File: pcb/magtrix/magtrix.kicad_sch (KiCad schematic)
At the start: 0 parts

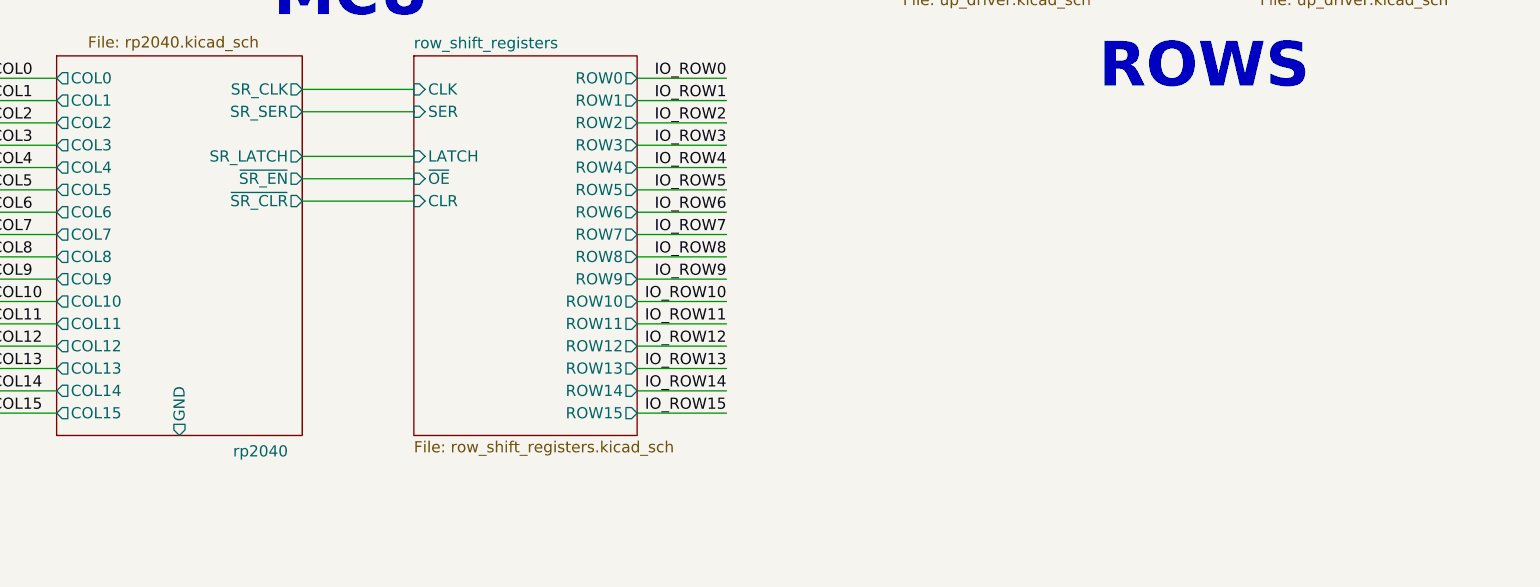
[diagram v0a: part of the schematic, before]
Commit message: Finished schematics and footprints, need to redo the placement
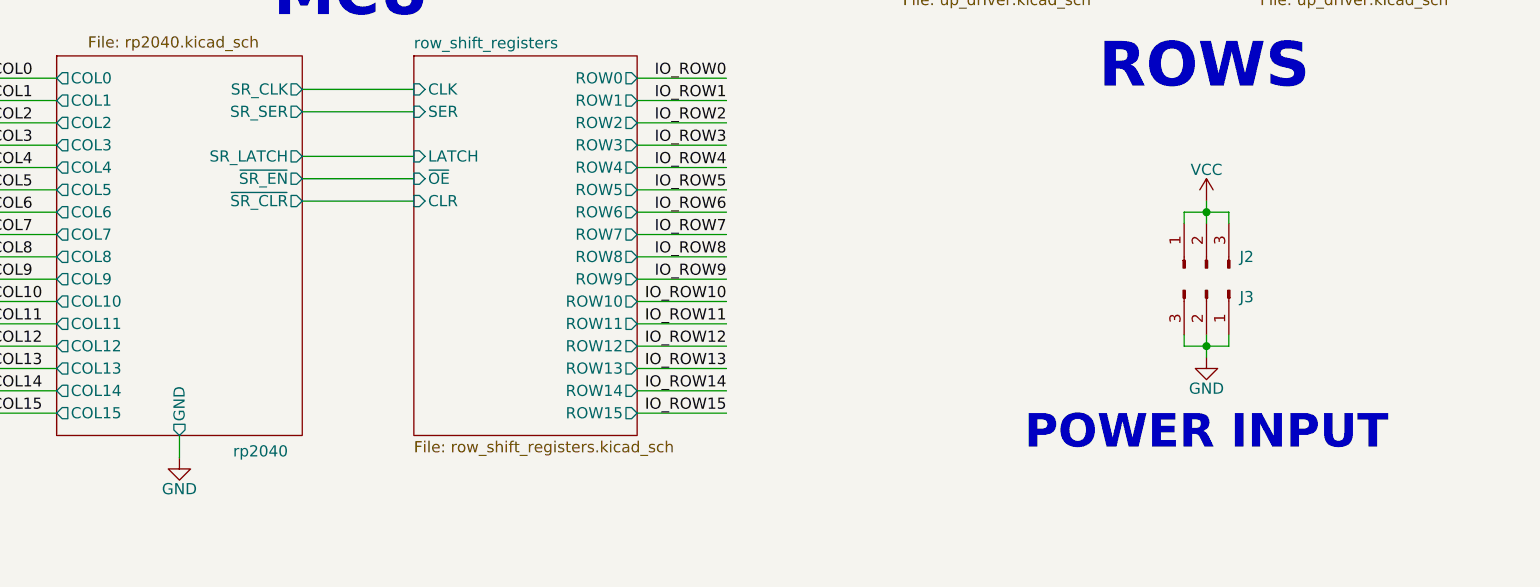
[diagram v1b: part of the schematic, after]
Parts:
- added J2, J3: Conn_01x03_Pin, Connector_PinHeader_2.54mm:PinHeader_1x03_P2.54mm_Vertical, symbol Connector:Conn_01x03_Pin
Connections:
- net GND: now also J3.1 (Pin_1), J3.2 (Pin_2), J3.3 (Pin_3)
- net VCC: now also J2.1 (Pin_1), J2.2 (Pin_2), J2.3 (Pin_3)
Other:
- note added: "POWER INPUT"

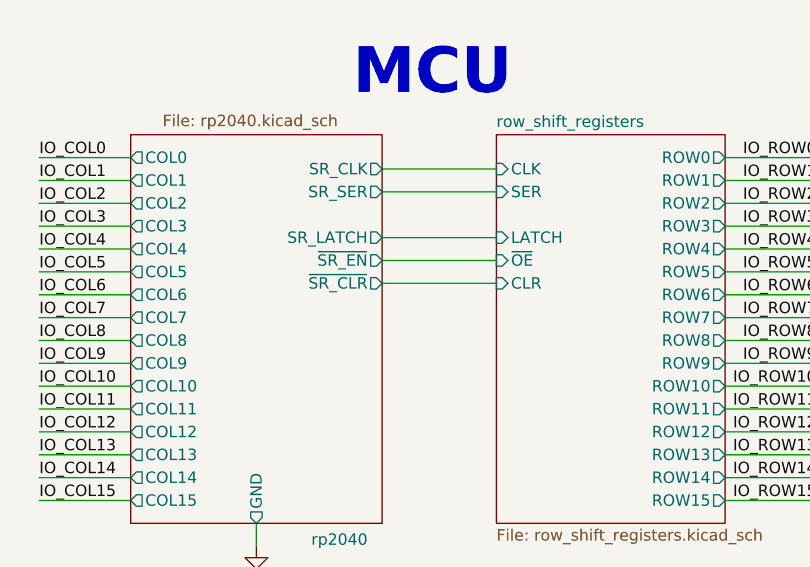
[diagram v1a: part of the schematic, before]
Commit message: Changed shift registers to open drain ones
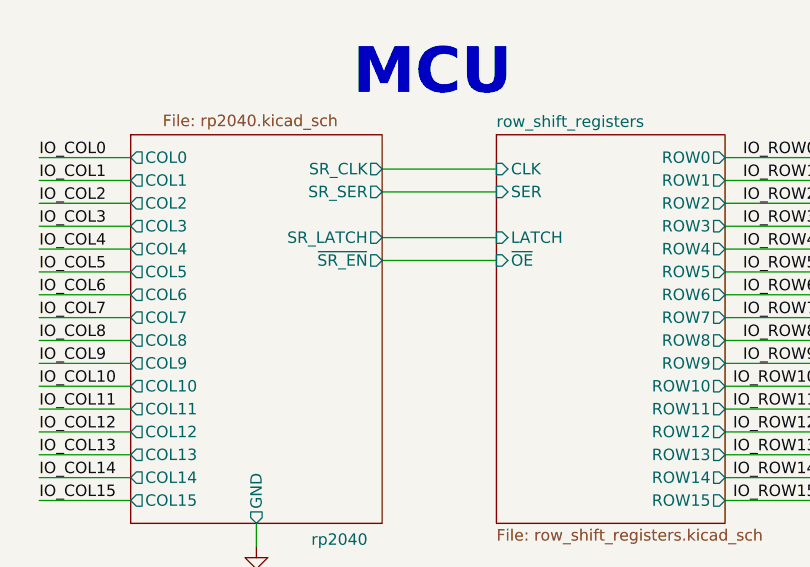
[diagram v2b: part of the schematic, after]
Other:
- sheet row_shift_registers ports: added none; removed CLR
- sheet rp2040 ports: added none; removed ~{SR_CLR}
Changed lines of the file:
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@@
 	(wire
 		(pts
-			(xy 143.51 130.81) (xy 156.21 130.81)
-		)
-		(stroke
-			(width 0)
-			(type default)
-		)
-	)
-	(wire
-		(pts
 			(xy 180.34 71.12) (xy 173.99 71.12)
 		)
@@
 			(project "magtrix"
 				(path "/11af7b42-8094-4ca6-9444-8e07a1921bec"
-					(page "5")
+					(page "38")
 				)
 			)
@@
 			)
 		)
-		(pin "CLR" input
-			(at 156.21 130.81 180)
-			(effects
-				(font
-					(size 1.27 1.27)
-				)
-				(justify left)
-			)
-		)
 		(pin "CLK" input
 			(at 156.21 118.11 180)
@@
 			(project "magtrix"
 				(path "/11af7b42-8094-4ca6-9444-8e07a1921bec"
-					(page "21")
+					(page "4")
 				)
 			)
@@
 			(project "magtrix"
 				(path "/11af7b42-8094-4ca6-9444-8e07a1921bec"
-					(page "4")
+					(page "37")
 				)
 			)
@@
 			)
 		)
-		(pin "~{SR_CLR}" output
-			(at 143.51 130.81 0)
-			(effects
-				(font
-					(size 1.27 1.27)
-				)
-				(justify right)
-			)
-		)
 		(pin "SR_CLK" output
 			(at 143.51 118.11 0)
@@
 			(project "magtrix"
 				(path "/11af7b42-8094-4ca6-9444-8e07a1921bec"
-					(page "37")
+					(page "5")
 				)
 			)

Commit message: Added finished PCB
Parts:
- added C1, C2, C20, C21, C22, C23, C24, C25, C26, C27, C28, C4, C5: 100u, BULK:CAPAE660X800N, symbol Device:C_Polarized_Small
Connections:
- net GND: now also C1.2, C2.2, C20.2, C21.2, C22.2, C23.2, C24.2, C25.2, C26.2, C27.2, C28.2, C4.2, C5.2
- net ROW_0: now also C1.1
- net ROW_1: now also C2.1
- net ROW_10: now also C26.1
- net ROW_11: now also C27.1
- net ROW_12: now also C28.1
- net ROW_2: now also C4.1
- net ROW_3: now also C5.1
- net ROW_4: now also C20.1
- net ROW_5: now also C21.1
- net ROW_6: now also C22.1
- net ROW_7: now also C23.1
- net ROW_8: now also C24.1
- net ROW_9: now also C25.1
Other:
- removed sheet BEMF
- removed sheet driver14
- removed sheet driver15
- removed sheet driver16
- removed sheet up_driver13
- removed sheet up_driver14
- removed sheet up_driver15
- added sheet flyback diodes (flyback_diodes.kicad_sch)
- sheet coil_matrix ports: added none; removed COL_13, COL_14, COL_15, ROW_13, ROW_14, ROW_15
- sheet row_shift_registers ports: added none; removed ROW13, ROW14, ROW15
- sheet rp2040 ports: added none; removed COL13, COL14, COL15
- note added: "Bulk capacitors"
- note added: "Flyback Diodes"
- note removed: "Back EMF Protections"
- title: (none) -> Magtrix Tic Tac Toe

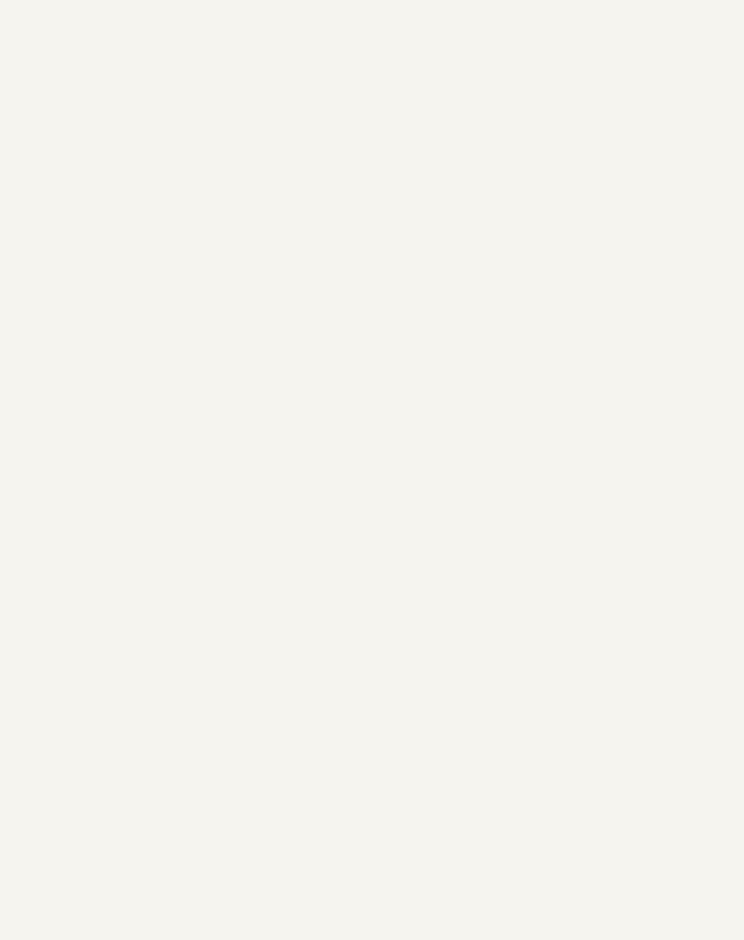
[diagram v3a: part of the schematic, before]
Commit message: Added debug pcb stuff
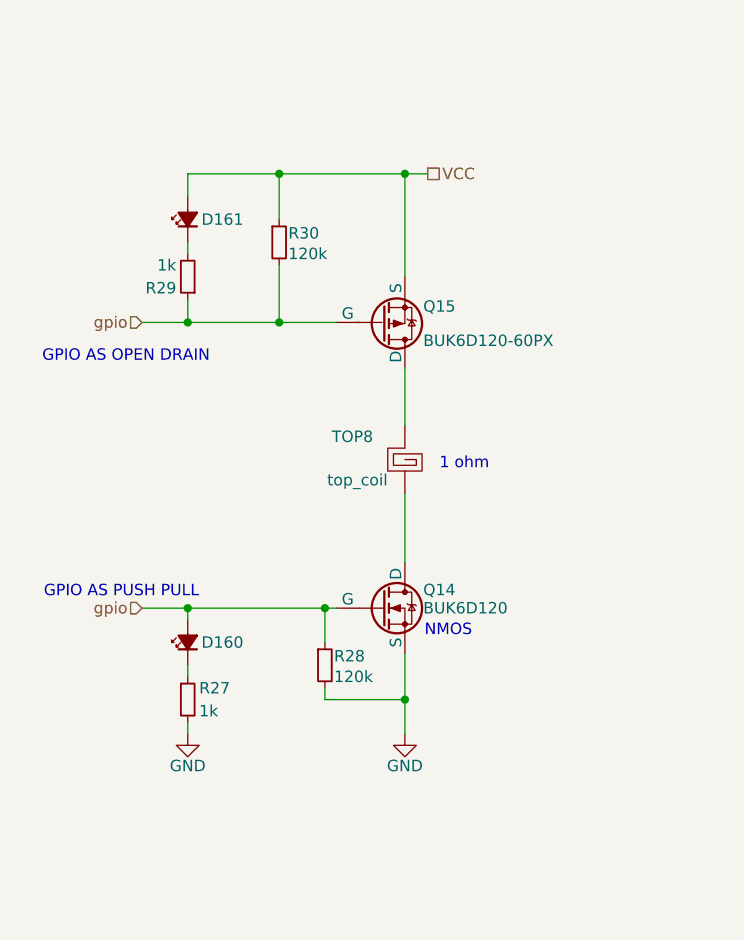
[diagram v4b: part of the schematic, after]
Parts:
- added D160, D161: LED_Small_Filled, LED_SMD:LED_1206_3216Metric, symbol Device:LED_Small_Filled
- added Q14: BUK6D120, TRANSISTOR_NMOS:TRANS_BUK9D23-40EX, symbol Simulation_SPICE:NMOS
- added Q15: BUK6D120-60PX, TRANSISTOR_PMOS:BUK6D12060PX, symbol Simulation_SPICE:PMOS
- added R27, R29: 1k, Resistor_SMD:R_1206_3216Metric, symbol Device:R_Small
- added R28, R30: 120k, Resistor_SMD:R_1206_3216Metric, symbol Device:R_Small
- added TOP8: top_coil, libs:top_coil, symbol square_coils:top_coil
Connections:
- net GND: now also Q14.4 (S), Q14.8 (S), R27.2, R28.2
- net VCC: now also D161.2 (A), Q15.4 (S), Q15.8 (S), R30.1
- new net: Q15.1 (D), Q15.2 (D), Q15.5 (D), Q15.6 (D), Q15.7 (D), TOP8.1 (A)
- new net: Q14.1 (D), Q14.2 (D), Q14.5 (D), Q14.6 (D), Q14.7 (D), TOP8.2 (B)
- new net: D160.1 (K), R27.1
- new net: D161.1 (K), R29.2
- new net gpio: D160.2 (A), Q14.3 (G), Q15.3 (G), R28.1, R29.1, R30.2
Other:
- note added: "1 ohm"
- note added: "GPIO AS OPEN DRAIN"
- note added: "GPIO AS PUSH PULL"
- note added: "NMOS"
